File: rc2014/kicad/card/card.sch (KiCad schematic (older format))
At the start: 19 parts

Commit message: Revision 2 w/ new level shifters
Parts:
- removed C? (x4): 100nF, symbol Device:C
- removed U? (x2): TXS0108EPW, Package_SO:TSSOP-20_4.4x6.5mm_P0.65mm, symbol Logic_LevelTranslator:TXS0108EPW
- added C? (x4): 100nF, symbol Device:C
- added U? (x2): SN74LVC8T245PWR, Package_SO:TSSOP-24_4.4x7.8mm_P0.65mm, symbol card:SN74LVC8T245PWR
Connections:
- net labels removed: A0, A1, A2, A3, A4, A5, A6, A7, D0, D1, D2, D3, D4, D5, D6, D7
- wire segments 153 -> 146
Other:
- note added: "2020-APRIL-12"
- note added: "REVISION 2"
- note removed: "2020-MARCH-29"
- note removed: "REVISION 1"
- moved on the sheet: C?, R?, SW?, U?

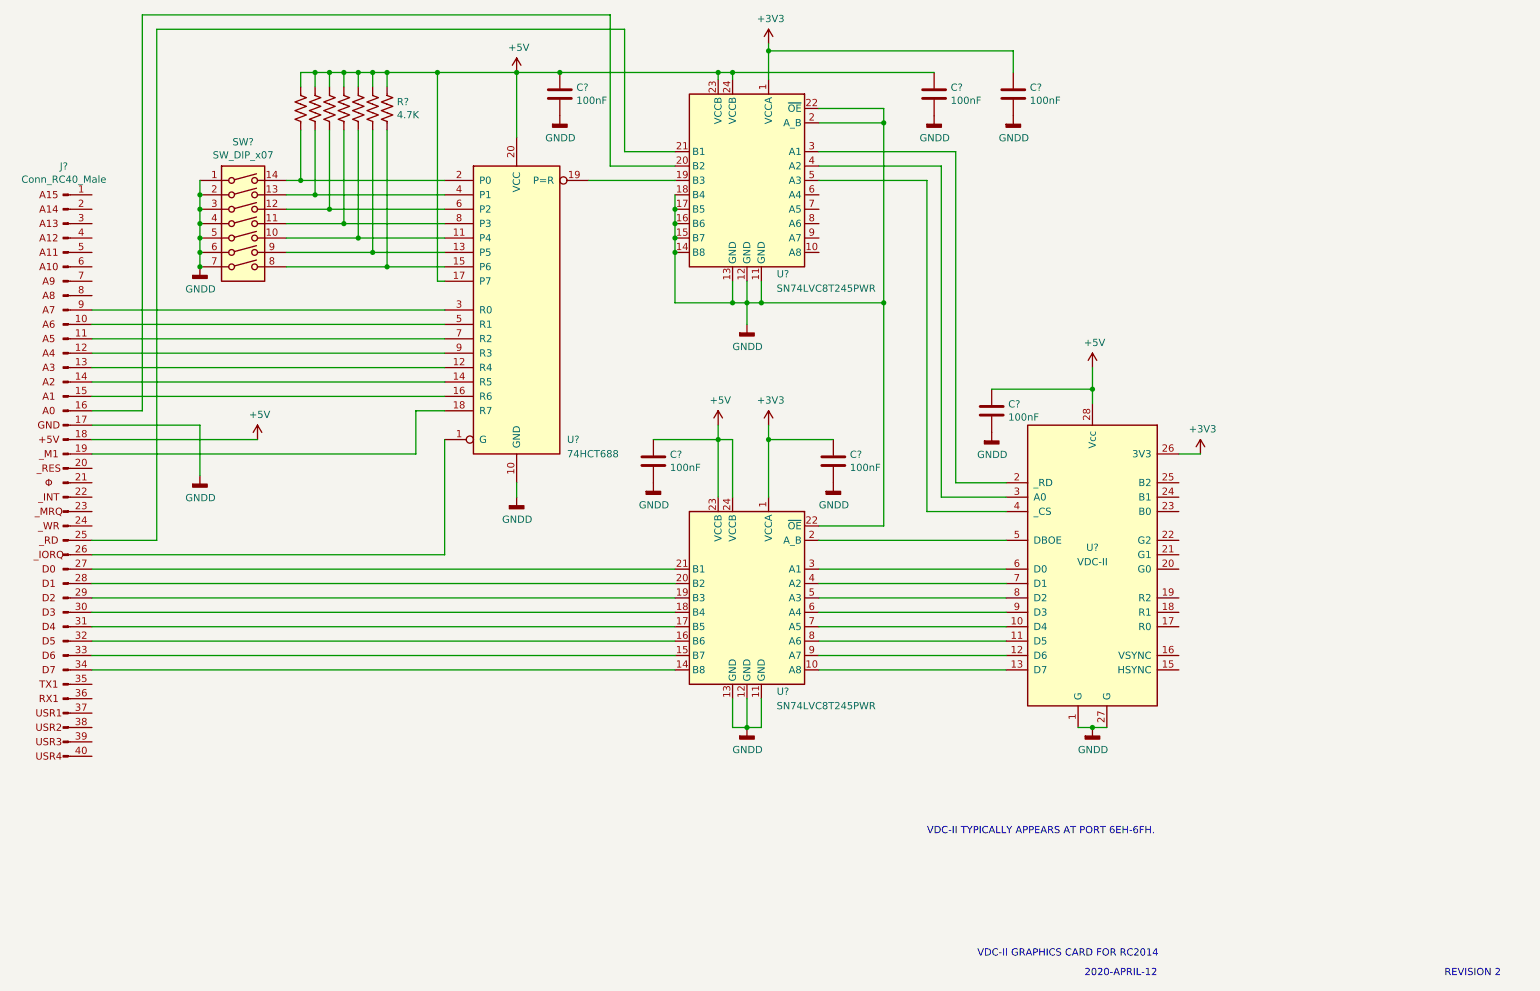
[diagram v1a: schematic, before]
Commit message: R4 schematic for VDC-II card
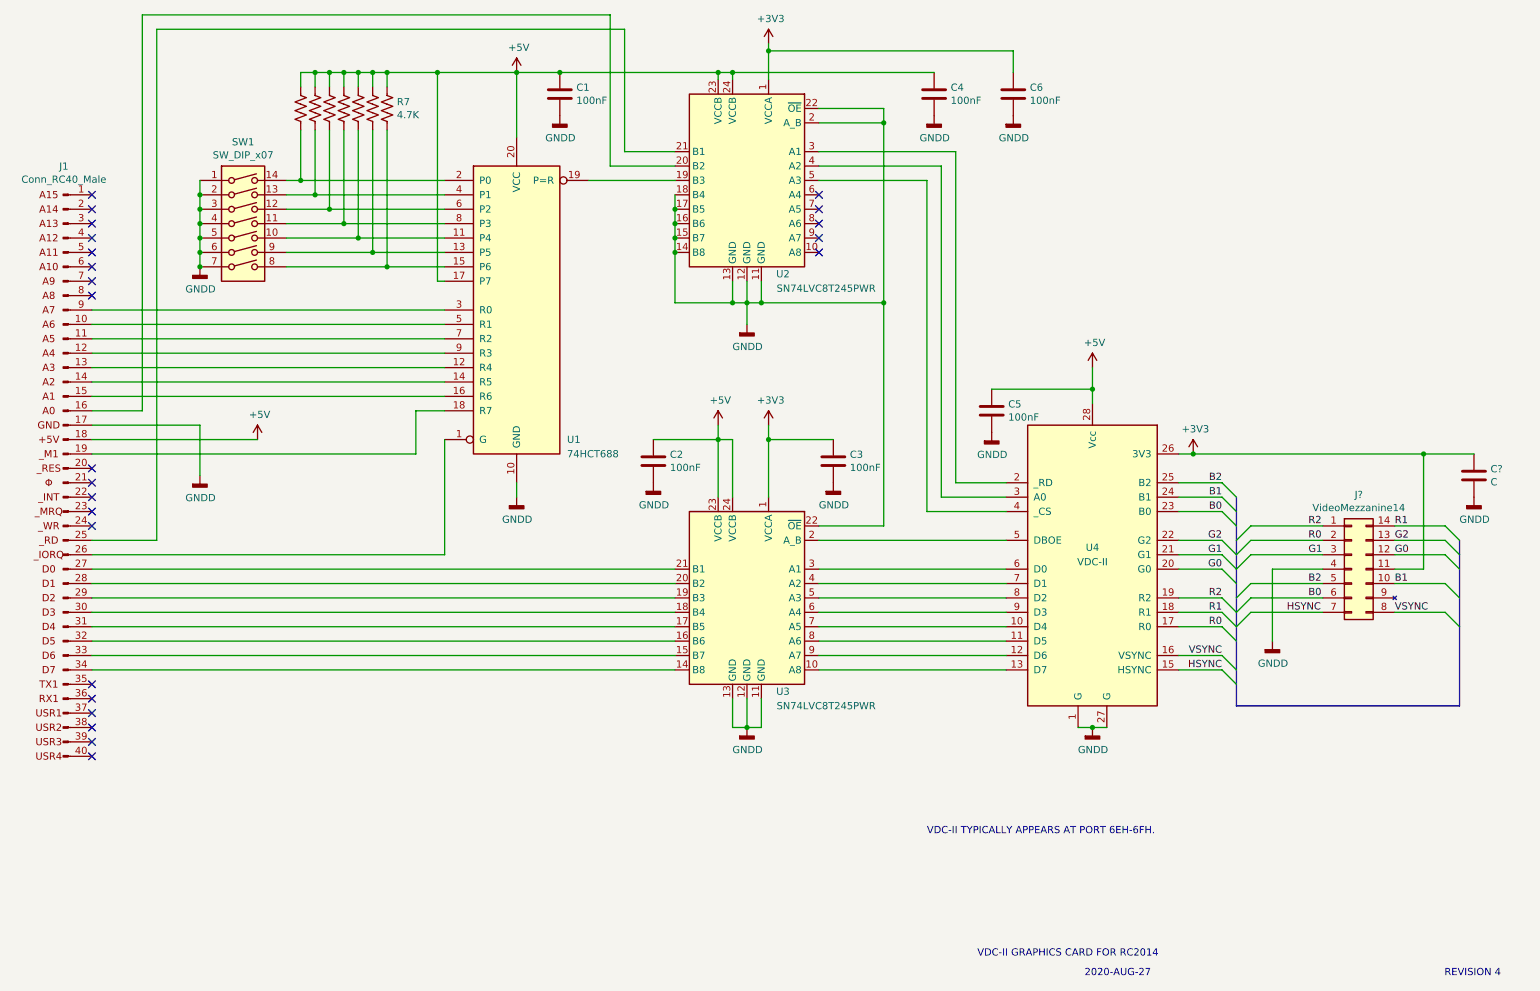
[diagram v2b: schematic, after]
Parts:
- added C?: C, symbol Device:C
- added J?: VideoMezzanine14, symbol card:VideoMezzanine14
- C1, C2, C3, C4, C5, C6: renamed from C?; footprint (none) -> Capacitor_THT:C_Disc_D6.0mm_W4.4mm_P5.00mm
- J1: renamed from J?; footprint (none) -> Connector_PinHeader_2.54mm:PinHeader_1x40_P2.54mm_Vertical
- R1, R2, R3, R4, R5, R6, R7: renamed from R?; footprint (none) -> Resistor_THT:R_Axial_DIN0207_L6.3mm_D2.5mm_P10.16mm_Horizontal
- SW1: renamed from SW?; footprint (none) -> Package_DIP:DIP-14_W10.16mm
- U1: renamed from U?; footprint (none) -> Package_DIP:DIP-20_W7.62mm_Socket
- U4: renamed from U?; footprint (none) -> Package_DIP:DIP-28_W15.24mm_Socket
- gave numbers to parts that had none: 2
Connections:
- net +3V3: now also C?.1, J?.11 (3V3)
- net GNDD: now also C?.2, J?.4 (GND)
- net HSYNC: now reaches U4.15 (HSYNC)
- net HSYNC: now also J?.7 (HSYNC)
- net VSYNC: now reaches U4.16 (VSYNC)
- net VSYNC: now also J?.8 (VSYNC)
- net R0: now reaches U4.17 (R0)
- net R0: now also J?.2 (R0)
- net R1: now reaches U4.18 (R1)
- net R1: now also J?.14 (R1)
- net R2: now reaches U4.19 (R2)
- net R2: now also J?.1 (R2)
- net G0: now reaches U4.20 (G0)
- net G0: now also J?.12 (G0)
- net G1: now reaches U4.21 (G1)
- net G1: now also J?.3 (G1)
- net G2: now reaches U4.22 (G2)
- net G2: now also J?.13 (G2)
- net B0: now reaches U4.23 (B0)
- net B0: now also J?.6 (B0)
- net B1: now reaches U4.24 (B1)
- net B1: now also J?.10 (B1)
- net B2: now reaches U4.25 (B2)
- net B2: now also J?.5 (B2)
- no-connect marks 0 -> 24
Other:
- note added: "2020-AUG-27"
- note added: "REVISION 4"
- note removed: "2020-APRIL-12"
- note removed: "REVISION 2"

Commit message: Repin U4
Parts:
- removed U4: VDC-II, Package_DIP:DIP-28_W15.24mm_Socket, symbol card:VDC-II
- added U4: VDC-II-card, Package_DIP:DIP-28_W15.24mm_Socket, symbol card-rescue:VDC-II-card
- C7: renamed from C?; footprint (none) -> Capacitor_THT:C_Disc_D6.0mm_W4.4mm_P5.00mm
- J2: renamed from J?; footprint (none) -> Package_DIP:DIP-14_W7.62mm_Socket
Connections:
- net +3V3: now also U4.26 (3V3)
- net +5V: now also U4.28 (Vcc)
- net B0: now also U4.23 (B0)
- net B1: now also U4.22 (B1)
- net B2: now also U4.21 (B2)
- net G0: now also U4.20 (G0)
- net G1: now also U4.19 (G1)
- net G2: now also U4.18 (G2)
- net GNDD: now also U4.1 (G), U4.27 (G)
- net HSYNC: now also U4.24 (HSYNC)
- net R0: now also U4.17 (R0)
- net R1: now also U4.16 (R1)
- net R2: now also U4.15 (R2)
- net VSYNC: now also U4.25 (VSYNC)
- net at U3.7 (A5): now also U4.10 (D4)
- net at U3.8 (A6): now also U4.11 (D5)
- net at U3.9 (A7): now also U4.12 (D6)
- net at U3.10 (A8): now also U4.13 (D7)
- net at U2.3 (A1): now also U4.2 (_RD)
- net at U2.4 (A2): now also U4.3 (A0)
- net at U2.5 (A3): now also U4.4 (_CS)
- net at U3.2 (A_B): now also U4.5 (DBOE)
- net at U3.3 (A1): now also U4.6 (D0)
- net at U3.4 (A2): now also U4.7 (D1)
- net at U3.5 (A3): now also U4.8 (D2)
- net at U3.6 (A4): now also U4.9 (D3)
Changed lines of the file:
@@
-$EndComp
-$Comp
-L card:VDC-II U4
-U 1 1 5E9C0017
-P 8200 4750
-F 0 "U4" H 8200 4850 50  0000 C CNN
-F 1 "VDC-II" H 8200 4750 50  0000 C CNN
-F 2 "Package_DIP:DIP-28_W15.24mm_Socket" H 8200 4750 50  0001 C CNN
-F 3 "" H 8200 4750 50  0001 C CNN
-	1    8200 4750
-	1    0    0    -1
 $EndComp
 $Comp
@@
 	9300 5100 9800 5100
 $Comp
-L power:GNDD #PWR?
+L power:GNDD #PWR0101
 U 1 1 5F5B660F
 P 9450 5300
-F 0 "#PWR?" H 9450 5050 50  0001 C CNN
+F 0 "#PWR0101" H 9450 5050 50  0001 C CNN
 F 1 "GNDD" H 9454 5145 50  0000 C CNN
 F 2 "" H 9450 5300 50  0001 C CNN
@@
 	10300 4900 10650 4900
 $Comp
-L card:VideoMezzanine14 J?
+L card:VideoMezzanine14 J2
 U 1 1 5F4F0374
 P 10000 4800
-F 0 "J?" H 10050 5317 50  0000 C CNN
+F 0 "J2" H 10050 5317 50  0000 C CNN
 F 1 "VideoMezzanine14" H 10050 5226 50  0000 C CNN
-F 2 "" H 10000 4800 50  0001 C CNN
+F 2 "Package_DIP:DIP-14_W7.62mm_Socket" H 10000 4800 50  0001 C CNN
 F 3 "~" H 10000 4800 50  0001 C CNN
 	1    10000 4800
@@
 VSYNC
 $Comp
-L Device:C C?
+L Device:C C7
 U 1 1 5F675DF6
 P 10850 4150
-F 0 "C?" H 10965 4196 50  0000 L CNN
+F 0 "C7" H 10965 4196 50  0000 L CNN
 F 1 "C" H 10965 4105 50  0000 L CNN
-F 2 "" H 10888 4000 50  0001 C CNN
+F 2 "Capacitor_THT:C_Disc_D6.0mm_W4.4mm_P5.00mm" H 10888 4000 50  0001 C CNN
 F 3 "~" H 10850 4150 50  0001 C CNN
 	1    10850 4150
@@
 Wire Wire Line
 	10500 4000 10850 4000
+Connection ~ 10500 4000
+$Comp
+L power:GNDD #PWR0102
+U 1 1 5F67EAA0
+P 10850 4300
+F 0 "#PWR0102" H 10850 4050 50  0001 C CNN
+F 1 "GNDD" H 10854 4145 50  0000 C CNN
+F 2 "" H 10850 4300 50  0001 C CNN
+F 3 "" H 10850 4300 50  0001 C CNN
+	1    10850 4300
+	1    0    0    -1
+$EndComp
+$Comp
+L card-rescue:VDC-II-card U4
+U 1 1 5F4BB38A
+P 8200 4750
+F 0 "U4" H 8350 5900 50  0000 C CNN
+F 1 "VDC-II-card" H 8550 5800 50  0000 C CNN
+F 2 "Package_DIP:DIP-28_W15.24mm_Socket" H 8200 4750 50  0001 C CNN
+F 3 "" H 8200 4750 50  0001 C CNN
+	1    8200 4750
+	1    0    0    -1
+$EndComp
 Wire Bus Line
 	10750 4600 10750 5750
 Wire Bus Line
 	9200 4300 9200 5750
-Connection ~ 10500 4000
-$Comp
-L power:GNDD #PWR?
-U 1 1 5F67EAA0
-P 10850 4300
-F 0 "#PWR?" H 10850 4050 50  0001 C CNN
-F 1 "GNDD" H 10854 4145 50  0000 C CNN
-F 2 "" H 10850 4300 50  0001 C CNN
-F 3 "" H 10850 4300 50  0001 C CNN
-	1    10850 4300
-	1    0    0    -1
-$EndComp
 $EndSCHEMATC

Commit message: Finish PCB layout for main PP board
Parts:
- C7: value C -> 100nF
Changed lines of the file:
@@
 P 10850 4150
 F 0 "C7" H 10965 4196 50  0000 L CNN
-F 1 "C" H 10965 4105 50  0000 L CNN
+F 1 "100nF" H 10965 4105 50  0000 L CNN
 F 2 "Capacitor_THT:C_Disc_D6.0mm_W4.4mm_P5.00mm" H 10888 4000 50  0001 C CNN
 F 3 "~" H 10850 4150 50  0001 C CNN

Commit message: Rev 4B of PCB layout.
- Fix missing pin 1 indicators.
- Fix missing 3.3V supply connection on U2.
- Fix DIP switch footprint size.
- Rename PCB to BX-PLORER
  - Pixel Pusher will be (BX-PLORER + VGA mezzanine).
  - Separate mezzanine planned for PS/2 keyboard and mouse.
- Convert J2 from 14-pin DIP to 14-pin female header.  (Same pinout
  though.)
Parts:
- J2: footprint Package_DIP:DIP-14_W7.62mm_Socket -> Connector_PinHeader_2.54mm:PinHeader_2x07_P2.54mm_Vertical; symbol card:VideoMezzanine14 -> Connector_Generic:Conn_02x07_Odd_Even
- SW1: footprint Package_DIP:DIP-14_W10.16mm -> Button_Switch_THT:SW_DIP_SPSTx07_Slide_9.78x19.96mm_W7.62mm_P2.54mm
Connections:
- net +3V3: now also J2.8 (Pin_8); no longer J2.11 (3V3)
- net B0: now also J2.11 (Pin_11); no longer J2.6 (B0)
- net B2: now also J2.9 (Pin_9); no longer J2.5 (B2)
- net G0: now also J2.6 (Pin_6); no longer J2.12 (G0)
- net G1: now also J2.5 (Pin_5); no longer J2.3 (G1)
- net G2: now also J2.4 (Pin_4); no longer J2.13 (G2)
- net GNDD: now also J2.7 (Pin_7); no longer J2.4 (GND)
- net HSYNC: now also J2.13 (Pin_13); no longer J2.7 (HSYNC)
- net R0: now also J2.3 (Pin_3); no longer J2.2 (R0)
- net R1: now also J2.2 (Pin_2); no longer J2.14 (R1)
- net VSYNC: now also J2.14 (Pin_14); no longer J2.8 (VSYNC)
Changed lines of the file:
@@
 F 0 "SW1" H 2300 3167 50  0000 C CNN
 F 1 "SW_DIP_x07" H 2300 3076 50  0000 C CNN
-F 2 "Package_DIP:DIP-14_W10.16mm" H 2300 2500 50  0001 C CNN
+F 2 "Button_Switch_THT:SW_DIP_SPSTx07_Slide_9.78x19.96mm_W7.62mm_P2.54mm" H 2300 2500 50  0001 C CNN
 F 3 "~" H 2300 2500 50  0001 C CNN
 	1    2300 2500
@@
 	10300 4900 10650 4900
 $Comp
-L card:VideoMezzanine14 J2
+L Connector_Generic:Conn_02x07_Odd_Even J2
 U 1 1 5F4F0374
 P 10000 4800
 F 0 "J2" H 10050 5317 50  0000 C CNN
 F 1 "VideoMezzanine14" H 10050 5226 50  0000 C CNN
-F 2 "Package_DIP:DIP-14_W7.62mm_Socket" H 10000 4800 50  0001 C CNN
+F 2 "Connector_PinHeader_2.54mm:PinHeader_2x07_P2.54mm_Vertical" H 10000 4800 50  0001 C CNN
 F 3 "~" H 10000 4800 50  0001 C CNN
 	1    10000 4800
